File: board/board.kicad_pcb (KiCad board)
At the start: 2 copper layers, 28 x 105 mm, 12 parts, among them U2 Adafruit_Feather_nRF52_Bluefr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

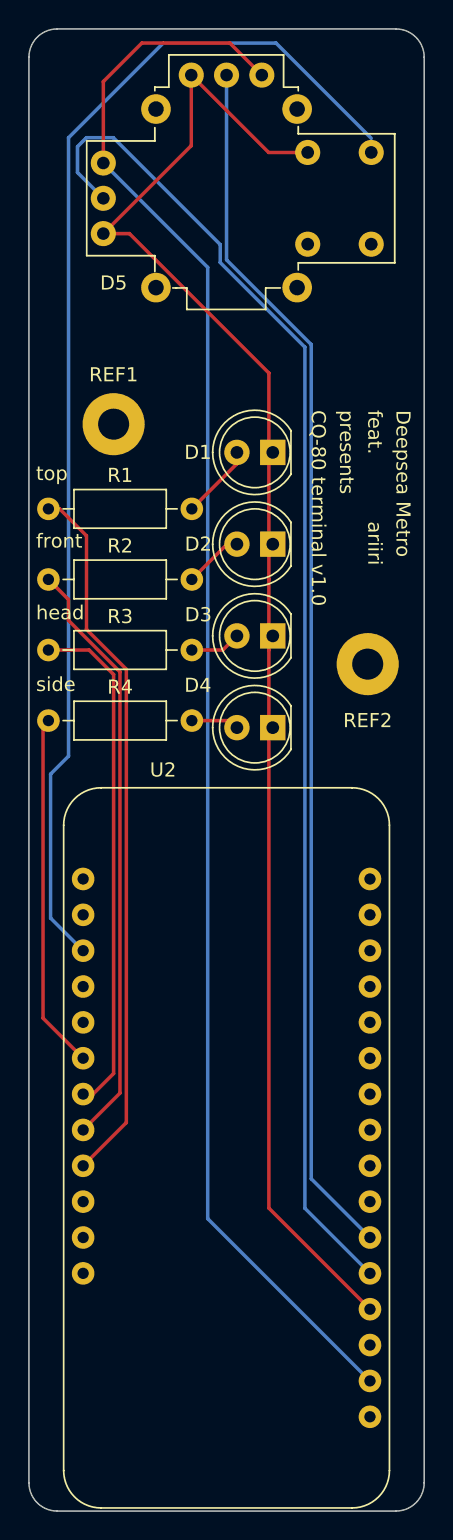
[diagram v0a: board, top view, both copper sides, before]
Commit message: * board: Add usb pin and second side light led
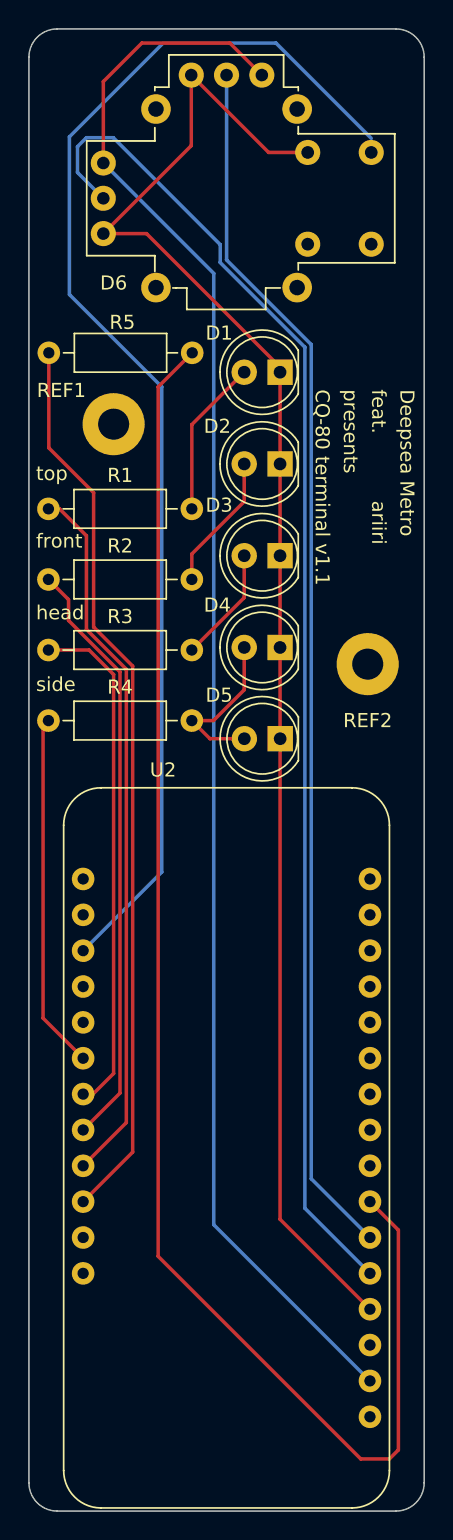
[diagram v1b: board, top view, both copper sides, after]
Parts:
- added D5: LED, LED_THT:LED_D5.0mm_Clear, F.Cu at (105.8, 95.3)
- added R5: R, Resistor_THT:R_Axial_DIN0207_L6.3mm_D2.5mm_P10.16mm_Horizontal, F.Cu at (99.6, 67.9)
- moved D1 5.70 mm to (105.8, 69.3)
- moved D2 5.70 mm to (105.8, 75.8)
- moved D3 5.70 mm to (105.8, 82.3)
- moved D4 5.70 mm to (105.8, 88.8)
- renumbered D5 to D6
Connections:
- U2 pad 26: unconnected-(U2-Pad26) -> Net-(U2-Pad26)
- U2 pad 7: unconnected-(U2-Pad7) -> Net-(U2-Pad7)
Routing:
- net Net-(U2-Pad7): track 0.00 -> 106.7 mm
- net Net-(U2-Pad26): track 0.00 -> 64.1 mm
- net Net-(D4-Pad2): track 3.40 -> 11.9 mm
- net Net-(D1-Pad2): track 5.32 -> 11.2 mm
- net Net-(D2-Pad2): track 4.23 -> 9.72 mm
- net Net-(D3-Pad2): track 3.61 -> 8.22 mm
- net Net-(D6-PadB1A): track 86.1 -> 89.6 mm
- net Net-(D1-Pad1): track 109.4 -> 110.1 mm
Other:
- board text added: "CQ-80 terminal v1.1"
- board text removed: "CQ-80 terminal v1.0"
